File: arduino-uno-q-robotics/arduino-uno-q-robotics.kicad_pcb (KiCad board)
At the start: 4 copper layers, 68.6 x 53.3 mm, 4 parts, among them J1 Conn_02x30_Odd_Even, J2 Conn_02x30_Odd_Even, J3 Connector_FFC-FPC, J4 Connector_FFC-FPC

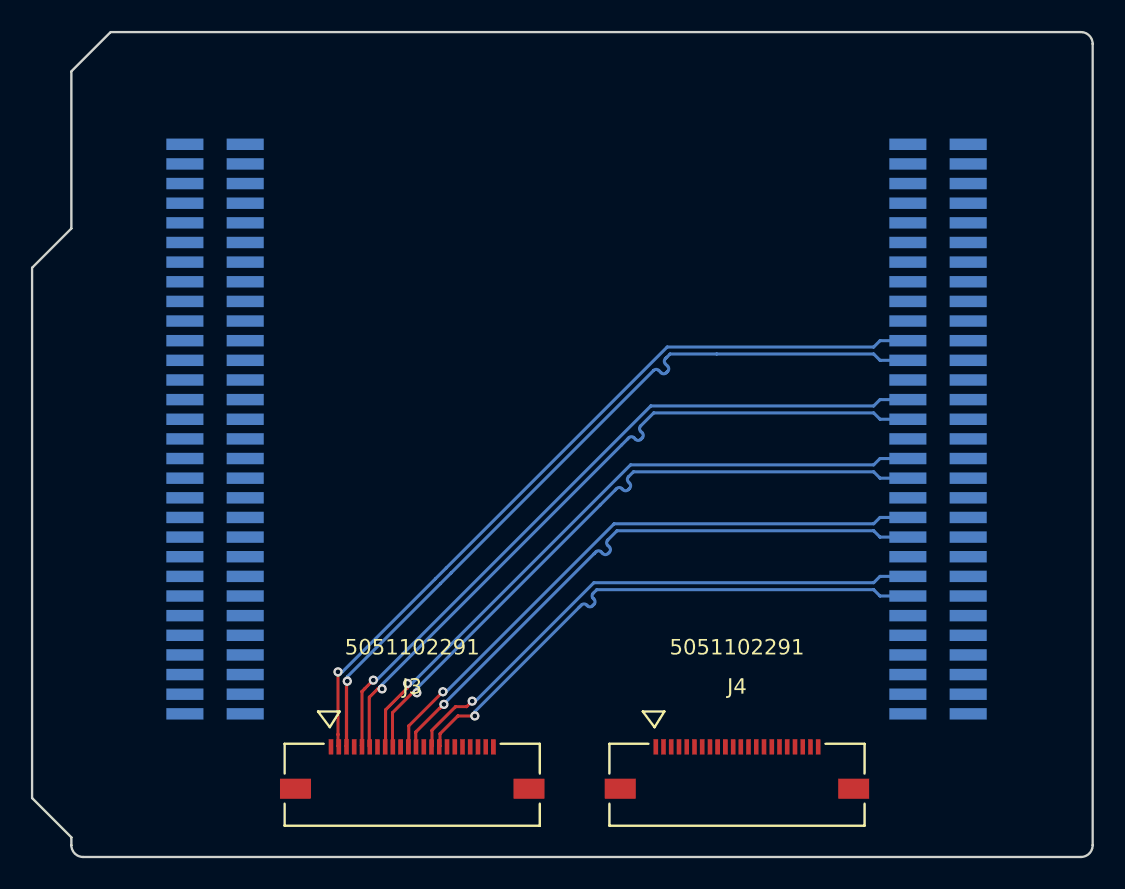
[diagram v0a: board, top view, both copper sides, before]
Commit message: Adjust Differential Pair values
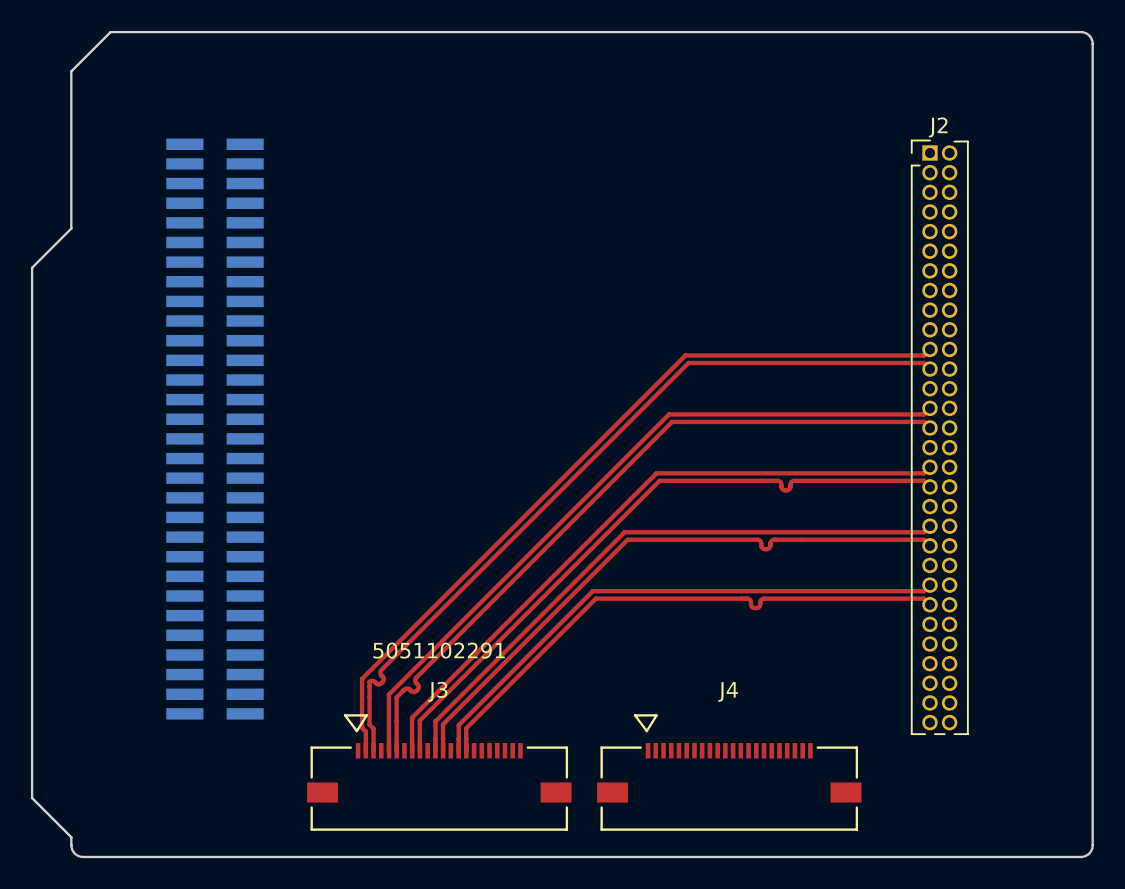
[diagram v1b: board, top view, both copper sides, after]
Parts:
- J2: footprint Connector_PinHeader_1.27mm:PinHeader_2x30_P1.27mm_Vertical_SMD -> Connector_PinHeader_1.27mm:PinHeader_2x30_P1.27mm_Vertical
- moved J2 17.9 mm to (172.5, 75.4)
- moved J3 1.77 mm to (140.8, 116.5)
- moved J4 0.56 mm to (159.5, 116.5)
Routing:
- net /CSI0_CLK_P: track 43.0 -> 42.3 mm, vias 1 -> 0
- net /CSI0_CLK_N: track 43.1 -> 42.3 mm, vias 1 -> 0
- net /CSI0_LN1_P: track 46.8 -> 46.3 mm, vias 1 -> 0
- net /CSI0_LN1_N: track 46.8 -> 46.3 mm, vias 1 -> 0
- net /CSI0_LN0_P: track 50.6 -> 50.3 mm, vias 1 -> 0
- net /CSI0_LN0_N: track 50.6 -> 50.3 mm, vias 1 -> 0
- net /CSI0_LN2_P: track 39.2 -> 39.1 mm, vias 1 -> 0
- net /CSI0_LN2_N: track 39.2 -> 39.1 mm, vias 1 -> 0
- net /CSI0_LN3_P: track 36.0 -> 35.8 mm, vias 1 -> 0
- net /CSI0_LN3_N: track 36.0 -> 35.9 mm, vias 1 -> 0

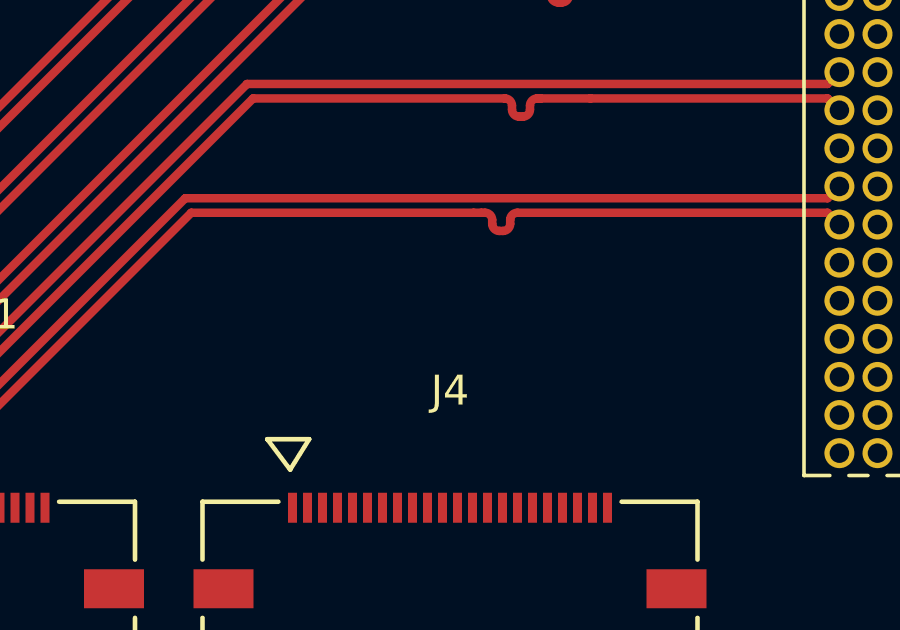
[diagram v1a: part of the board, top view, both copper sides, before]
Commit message: Separate camera connectors level shifter
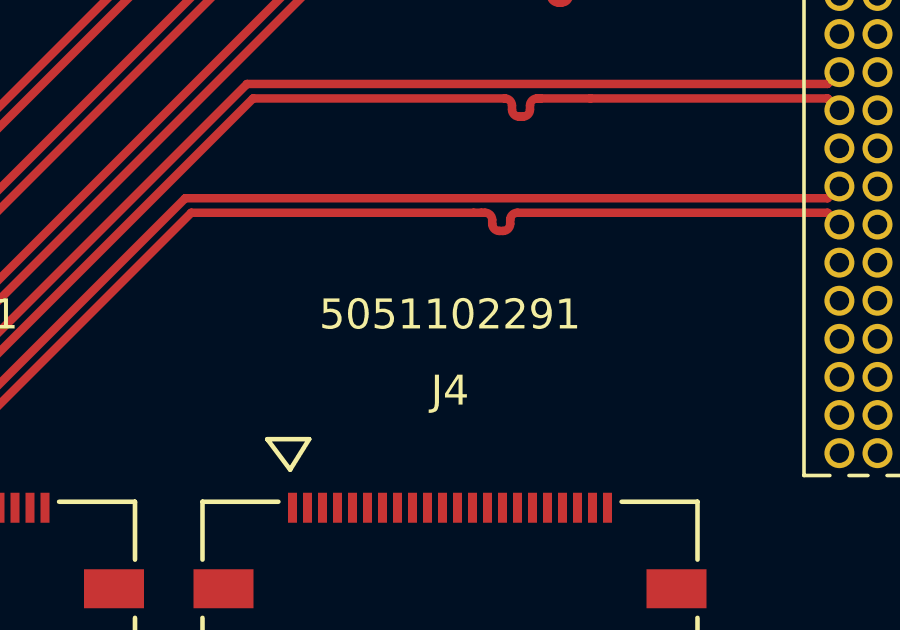
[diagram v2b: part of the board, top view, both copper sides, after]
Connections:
- J3 pad 20: /SCL_3.3V -> /SCL0_3.3V
- J3 pad 21: /SDA_3.3V -> /SDA0_3.3V
- J4 pad 20: /SCL_3.3V -> /SCL1_3.3V
- J4 pad 21: /SDA_3.3V -> /SDA1_3.3V
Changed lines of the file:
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@@
 	(net 64 "VBAT")
 	(net 65 "+3V3")
-	(net 66 "/SDA_3.3V")
+	(net 66 "/SCL0_3.3V")
 	(net 67 "unconnected-(J3-Pad17)")
 	(net 68 "unconnected-(J3-Pad18)")
-	(net 69 "/SCL_3.3V")
+	(net 69 "/SDA0_3.3V")
 	(net 70 "unconnected-(J4-Pad17)")
 	(net 71 "unconnected-(J4-Pad18)")
@@
 	(net 101 "/CSI0_CLK_P")
 	(net 102 "/CSI0_LN2_P")
+	(net 103 "/SDA1_3.3V")
+	(net 104 "/SCL1_3.3V")
 	(footprint "robotics-footprints:CON_5051102291_MOL"
 		(layer "F.Cu")
@@
 			(layer "F.Fab")
 		)
+		(fp_text user "5051102291"
+			(at 0 -8.89 0)
+			(unlocked yes)
+			(layer "F.SilkS")
+			(effects
+				(font
+					(size 1 1)
+					(thickness 0.15)
+				)
+			)
+		)
 		(fp_text user "${REFERENCE}"
 			(at 0 -6.35 0)
@@
 			)
 		)
+		(fp_text user "5051102291"
+			(at 0 -8.89 0)
+			(unlocked yes)
+			(layer "F.Fab")
+			(effects
+				(font
+					(size 1 1)
+					(thickness 0.15)
+				)
+			)
+		)
 		(pad "1" smd rect
 			(at -5.25 -2.45)
@@
 			(size 0.3 1)
 			(layers "F.Cu" "F.Mask" "F.Paste")
-			(net 69 "/SCL_3.3V")
+			(net 104 "/SCL1_3.3V")
 			(pinfunction "20")
 			(pintype "unspecified")
@@
 			(size 0.3 1)
 			(layers "F.Cu" "F.Mask" "F.Paste")
-			(net 66 "/SDA_3.3V")
+			(net 103 "/SDA1_3.3V")
 			(pinfunction "21")
 			(pintype "unspecified")
@@
 			(size 0.3 1)
 			(layers "F.Cu" "F.Mask" "F.Paste")
-			(net 69 "/SCL_3.3V")
+			(net 66 "/SCL0_3.3V")
 			(pinfunction "20")
 			(pintype "unspecified")
@@
 			(size 0.3 1)
 			(layers "F.Cu" "F.Mask" "F.Paste")
-			(net 66 "/SDA_3.3V")
+			(net 69 "/SDA0_3.3V")
 			(pinfunction "21")
 			(pintype "unspecified")

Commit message: Add a 3.3v power layer
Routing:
- added copper zone on In2.Cu, net +3.3V
- removed copper zone on In2.Cu, net GND
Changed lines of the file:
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@@
 		(net 5)
 		(net_name "GND")
-		(layers "In1.Cu" "In2.Cu")
+		(layer "In1.Cu")
 		(hatch edge 0.5)
 		(connect_pads
@@
 			)
 		)
+	)
+	(zone
+		(net 62)
+		(net_name "+3.3V")
+		(layer "In2.Cu")
+		(hatch edge 0.5)
+		(priority 1)
+		(connect_pads
+			(clearance 0.4)
+		)
+		(min_thickness 0.25)
+		(filled_areas_thickness no)
+		(fill yes
+			(thermal_gap 0.5)
+			(thermal_bridge_width 0.5)
+		)
+		(polygon
+			(pts
+				(xy 185.5 122.75) (xy 185.5 64.5) (xy 185 64) (xy 115.5 64) (xy 111.25 68.25) (xy 111.25 121.25)
+				(xy 112.75 122.75)
+			)
+		)

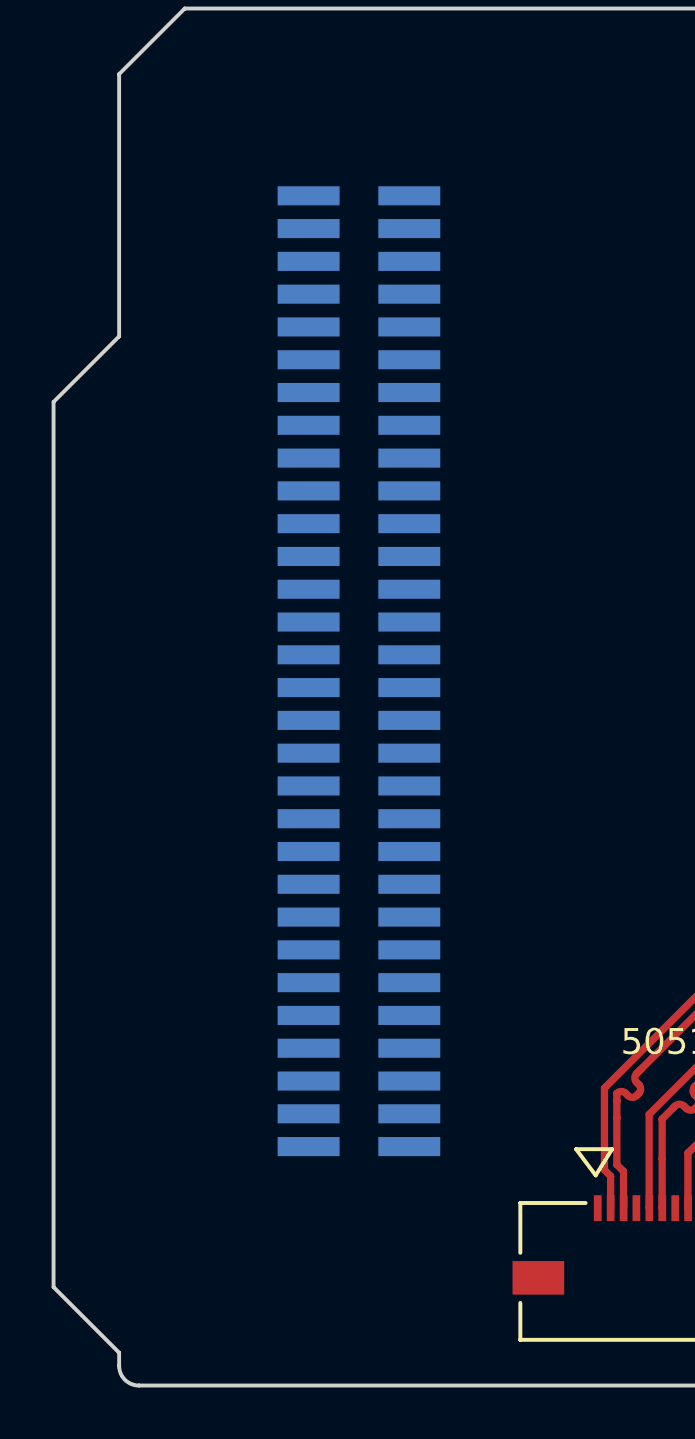
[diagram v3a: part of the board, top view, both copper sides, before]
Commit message: Add Pin sockets and headers for JMISC pins
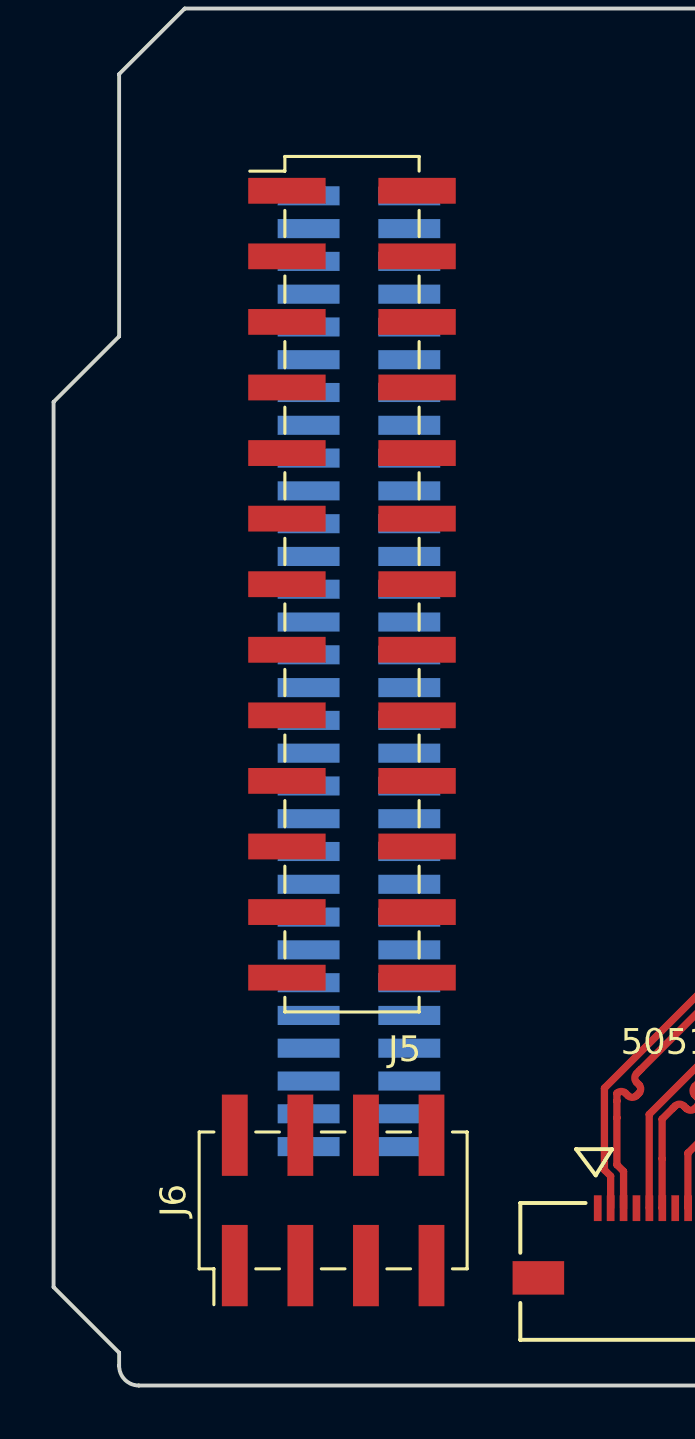
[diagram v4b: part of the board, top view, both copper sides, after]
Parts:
- added J5: Conn_02x13_Odd_Even, Connector_PinSocket_2.54mm:PinSocket_2x13_P2.54mm_Vertical_SMD, F.Cu at (126.1, 89.9)
- added J6: Conn_02x04_Odd_Even, Connector_PinHeader_2.54mm:PinHeader_2x04_P2.54mm_Vertical_SMD, F.Cu at (125.2, 113.8)
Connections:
- J1 pad 26: unconnected-(J1-Pin_26-Pad26) -> VBAT

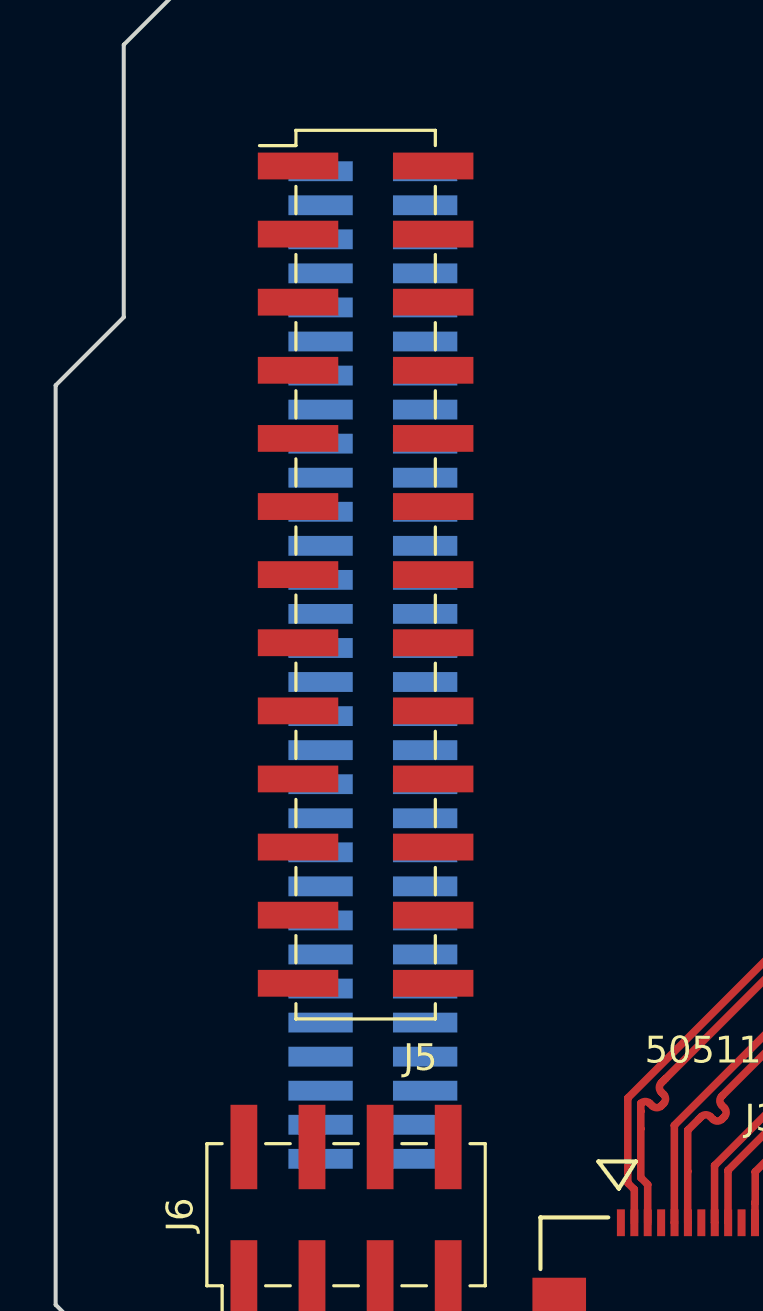
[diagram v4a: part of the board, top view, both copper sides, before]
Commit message: Add trace connections to JMISC 2.54 header
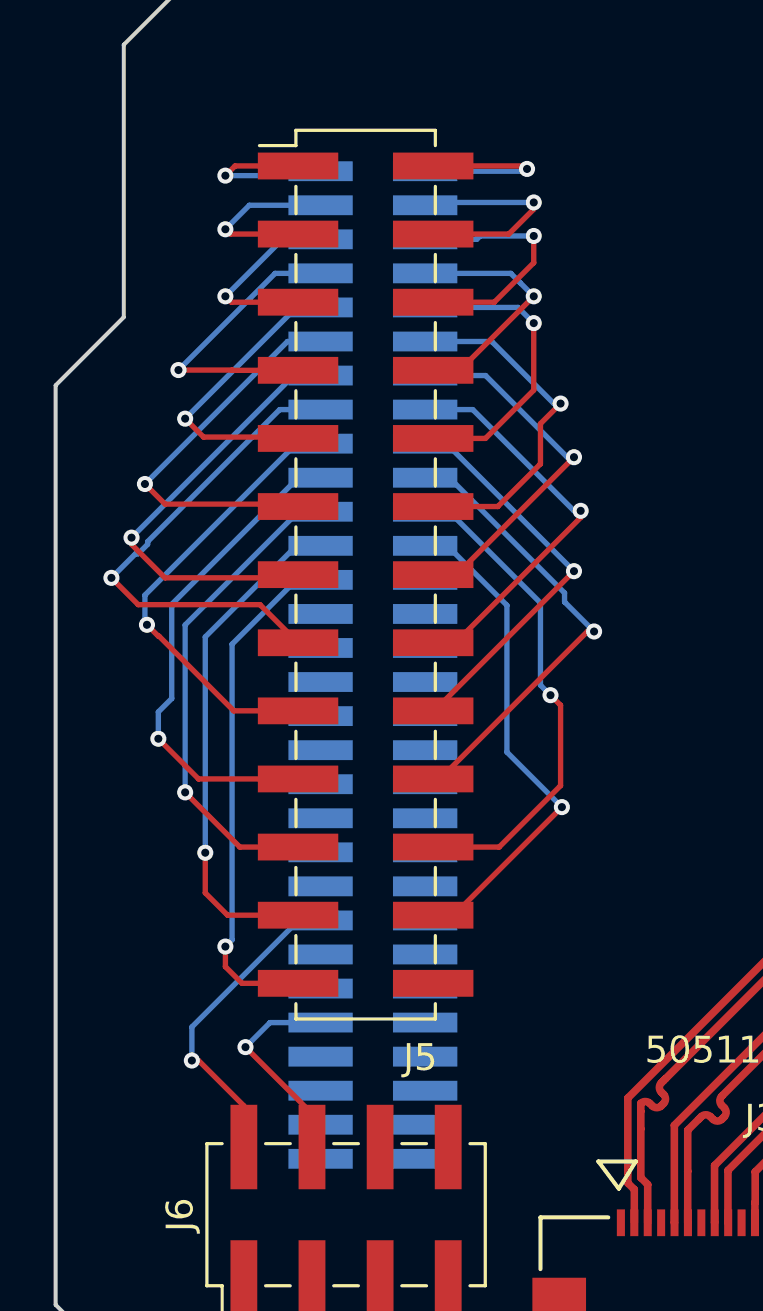
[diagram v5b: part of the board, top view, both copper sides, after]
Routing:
- net /MCU_CRS_SYNC: track 0.00 -> 19.4 mm, vias 0 -> 1
- net /MCU_MCO: track 0.00 -> 19.1 mm, vias 0 -> 1
- net /MCU_OPAMP1_VINM: track 0.00 -> 18.8 mm, vias 0 -> 1
- net /MCU_PSSI_RDY: track 0.00 -> 18.6 mm, vias 0 -> 1
- net /MCU_OPAMP1_VINP: track 0.00 -> 18.5 mm, vias 0 -> 1
- net /MCU_PSSI_D7: track 0.00 -> 18.4 mm, vias 0 -> 1
- net /MCU_PSSI_DE: track 0.00 -> 18.1 mm, vias 0 -> 1
- net /MCU_OPAMP1_VOUT: track 0.00 -> 17.2 mm, vias 0 -> 1
- net /MCU_PSSI_PDCK: track 0.00 -> 17.0 mm, vias 0 -> 1
- net /MCU_PSSI_D6: track 0.00 -> 16.6 mm, vias 0 -> 1
- net /MCU_I2C4_SCL: track 0.00 -> 15.0 mm, vias 0 -> 1
- net /MCU_I2C4_SDA: track 0.00 -> 14.9 mm, vias 0 -> 1
- net /MCU_PSSI_D5: track 0.00 -> 14.8 mm, vias 0 -> 1
- net /MCU_PE8: track 0.00 -> 13.9 mm, vias 0 -> 1
- net /MCU_PE7: track 0.00 -> 13.2 mm, vias 0 -> 1
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
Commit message: Connect magnet and stemma port
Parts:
- added R1: 10k, Resistor_SMD:R_0603_1608Metric_Pad0.98x0.95mm_HandSolder, F.Cu at (138.0, 87.2)
- added R2: 10k, Resistor_SMD:R_0603_1608Metric_Pad0.98x0.95mm_HandSolder, F.Cu at (138.0, 90.0)
- added R3: 10k, Resistor_SMD:R_0603_1608Metric_Pad0.98x0.95mm_HandSolder, F.Cu at (141.0, 78.2)
- added U1: LSM6DSO32, robotics-footprints:LGA-14L_2P5X3X0P83_STM, F.Cu at (141.8, 82.5)
- added U3: ~, Connector_JST:JST_SH_SM04B-SRSS-TB_1x04-1MP_P1.00mm_Horizontal, F.Cu at (136.8, 71.6)
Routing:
- net /MCU_I2C4_SDA: track 14.9 -> 40.1 mm, vias 1 -> 3
- net /MCU_I2C4_SCL: track 15.0 -> 37.7 mm
- net +3.3V: track 0.00 -> 10.5 mm, vias 0 -> 4
- net GND: track 0.00 -> 5.17 mm, vias 0 -> 2
- net /CS: track 0.00 -> 3.39 mm
- net /MCU_PE7: track 13.2 -> 12.3 mm
